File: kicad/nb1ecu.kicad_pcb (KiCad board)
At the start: 2 copper layers, 154 x 159 mm, 2 parts, among them P2 178780-1, U1 Teensy4.1

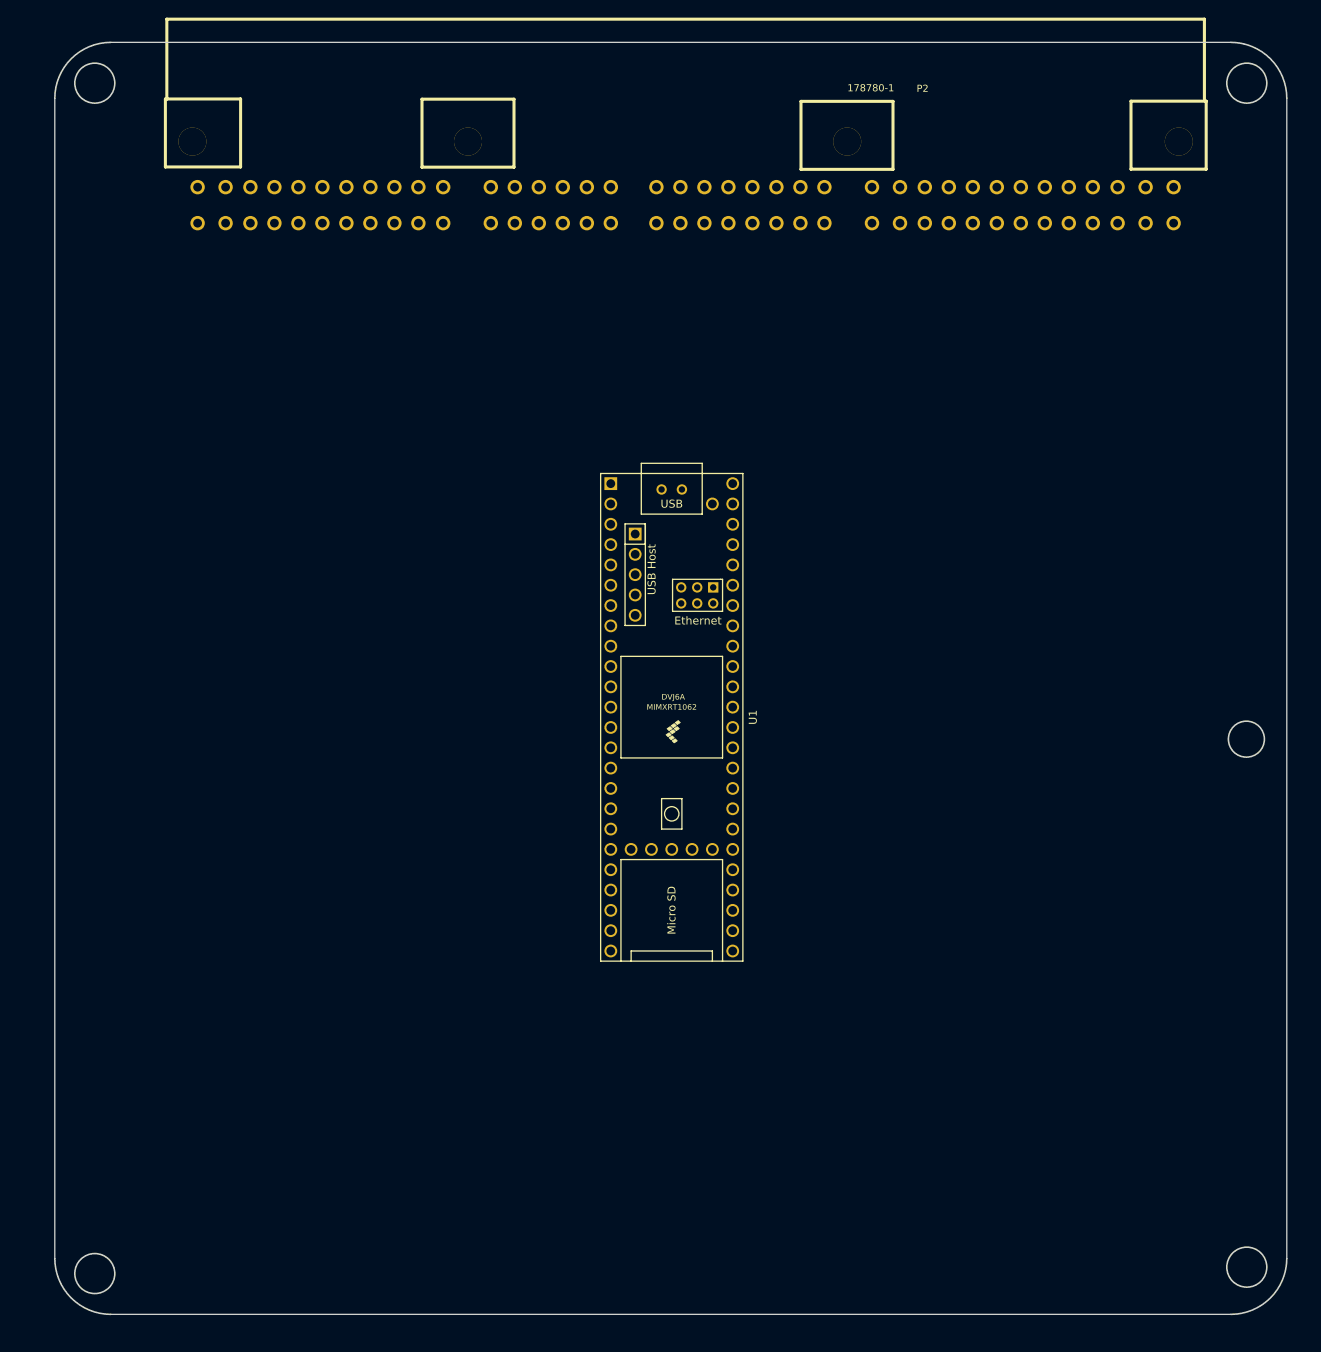
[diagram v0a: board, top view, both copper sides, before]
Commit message: ready to test, need to add part numbers for bom
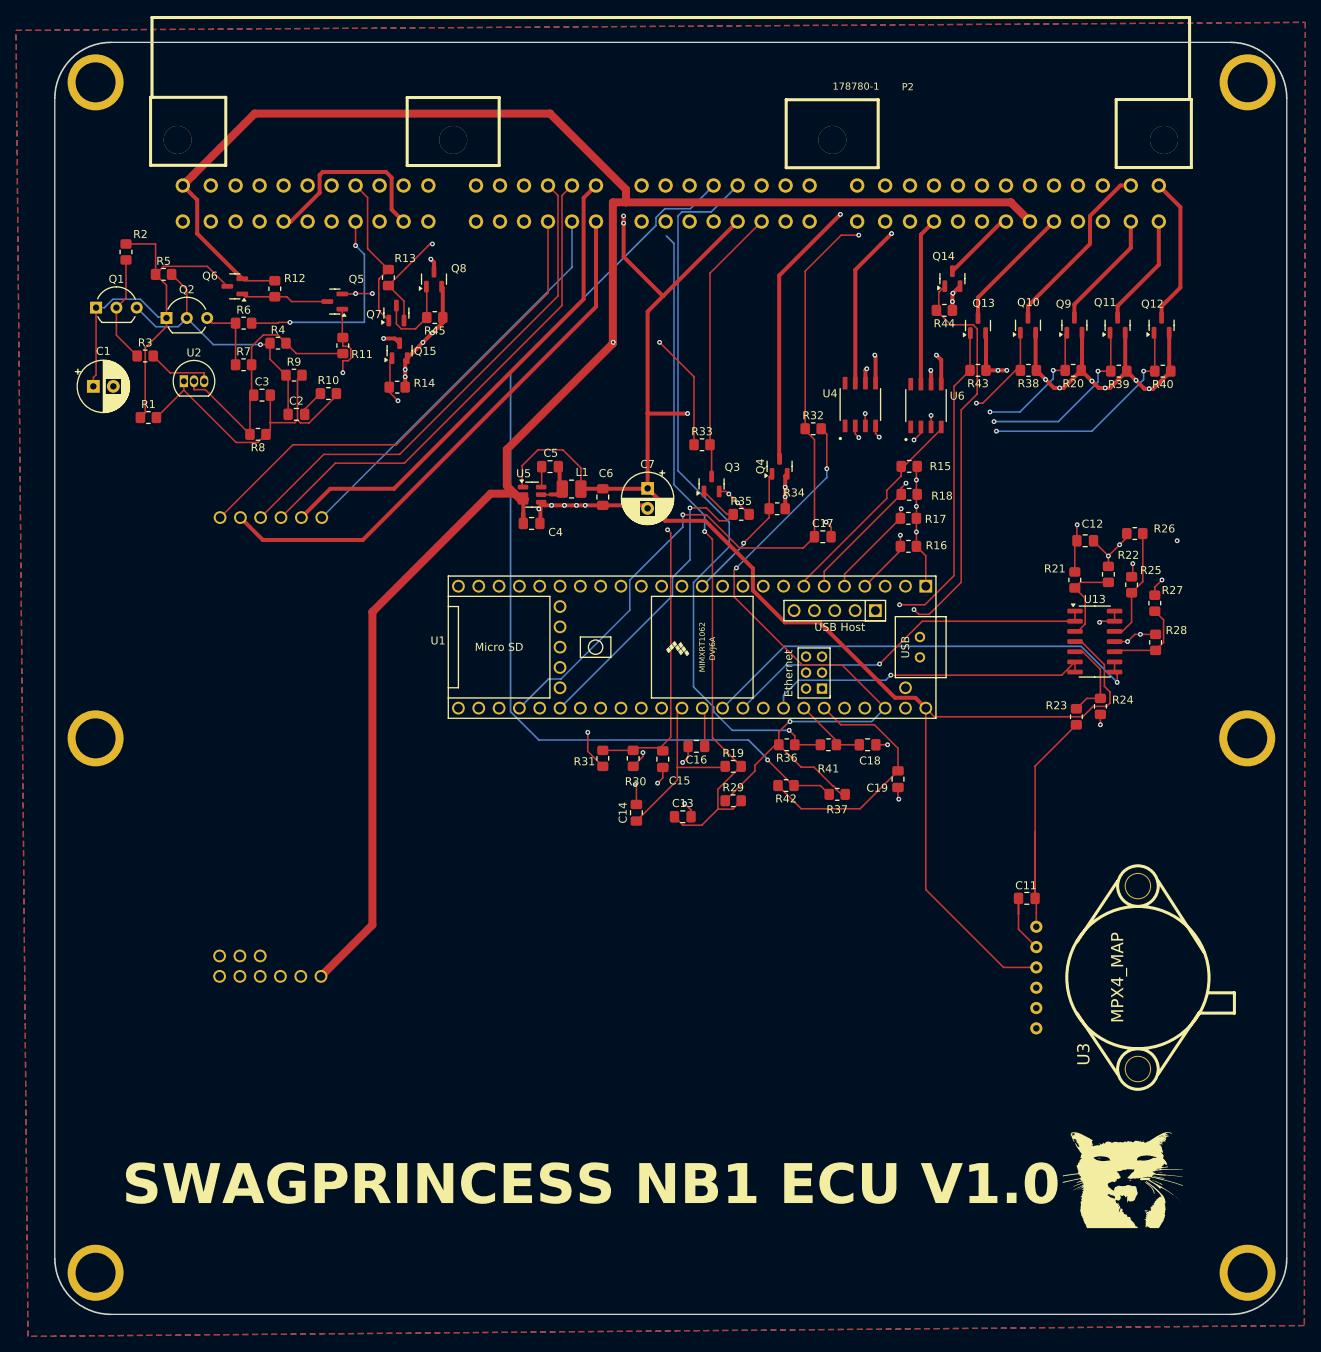
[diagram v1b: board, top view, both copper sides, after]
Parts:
- added C1: 100u, Capacitor_THT:CP_Radial_D6.3mm_P2.50mm, F.Cu at (23.4, 62.0)
- added C11: 470n, Capacitor_SMD:C_0805_2012Metric_Pad1.18x1.45mm_HandSolder, F.Cu at (140.1, 126.0)
- added C12: 220n, Capacitor_SMD:C_0805_2012Metric_Pad1.18x1.45mm_HandSolder, F.Cu at (147.4, 81.3)
- added C13: 100n, Capacitor_SMD:C_0805_2012Metric_Pad1.18x1.45mm_HandSolder, F.Cu at (97.1, 115.8)
- added C14: 220n, Capacitor_SMD:C_0805_2012Metric_Pad1.18x1.45mm_HandSolder, F.Cu at (91.3, 115.3)
- added C15: 100n, Capacitor_SMD:C_0805_2012Metric_Pad1.18x1.45mm_HandSolder, F.Cu at (94.6, 108.6)
- added C16: 220n, Capacitor_SMD:C_0805_2012Metric_Pad1.18x1.45mm_HandSolder, F.Cu at (98.8, 107.0)
- added C17: 220n, Capacitor_SMD:C_0805_2012Metric_Pad1.18x1.45mm_HandSolder, F.Cu at (114.6, 80.8)
- added C18: 100n, Capacitor_SMD:C_0805_2012Metric_Pad1.18x1.45mm_HandSolder, F.Cu at (120.2, 106.8)
- added C19: 100n, Capacitor_SMD:C_0805_2012Metric_Pad1.18x1.45mm_HandSolder, F.Cu at (124.0, 111.1)
- added C2: 22n, Capacitor_SMD:C_0805_2012Metric_Pad1.18x1.45mm_HandSolder, F.Cu at (48.8, 65.5)
- added C3: 1n, Capacitor_SMD:C_0805_2012Metric_Pad1.18x1.45mm_HandSolder, F.Cu at (44.5, 63.1)
- added C4: 10u, Capacitor_SMD:C_0805_2012Metric_Pad1.18x1.45mm_HandSolder, F.Cu at (78.2, 79.1)
- added C5: 100n, Capacitor_SMD:C_0805_2012Metric_Pad1.18x1.45mm_HandSolder, F.Cu at (80.5, 72.0)
- added C6: 10u, Capacitor_SMD:C_0805_2012Metric_Pad1.18x1.45mm_HandSolder, F.Cu at (87.1, 75.8)
- added C7: 100u, Capacitor_THT:CP_Radial_D6.3mm_P2.50mm, F.Cu at (92.7, 74.8)
- added J11: Conn_01x01, MountingHole:MountingHole_4.5mm_Pad, F.Cu at (23.7, 24.0)
- added J13: Conn_01x01, MountingHole:MountingHole_4.5mm_Pad, F.Cu at (23.7, 172.8)
- added J14: Conn_01x01, MountingHole:MountingHole_4.5mm_Pad, F.Cu at (167.7, 172.8)
- added J15: Conn_01x01, MountingHole:MountingHole_4.5mm_Pad, F.Cu at (167.7, 106.0)
- added J16: Conn_01x01, MountingHole:MountingHole_4.5mm_Pad, F.Cu at (167.7, 24.0)
- added J17: Conn_01x01, MountingHole:MountingHole_4.5mm_Pad, F.Cu at (23.7, 106.0)
- added L1: 4.7u, Inductor_SMD:L_1008_2520Metric_Pad1.43x2.20mm_HandSolder, F.Cu at (83.2, 74.8)
- added Q1: PN2907A, Package_TO_SOT_THT:TO-92_Inline_Wide, F.Cu at (23.8, 52.2)
- added Q10: DMG2302U, Package_TO_SOT_SMD:SOT-23, F.Cu at (140.2, 54.4)
- added Q11: DMG2302U, Package_TO_SOT_SMD:SOT-23, F.Cu at (151.4, 54.4)
- added Q12: DMG2302U, Package_TO_SOT_SMD:SOT-23, F.Cu at (156.9, 54.4)
- added Q13: DMG2302U, Package_TO_SOT_SMD:SOT-23, F.Cu at (134.0, 54.4)
- added Q14: DMG2302U, Package_TO_SOT_SMD:SOT-23, F.Cu at (130.8, 48.5)
- added Q15: DMG2302U, Package_TO_SOT_SMD:SOT-23, F.Cu at (61.7, 57.5)
- added Q2: PN2907A, Package_TO_SOT_THT:TO-92_Inline_Wide, F.Cu at (32.6, 53.5)
- added Q3: DMG2302U, Package_TO_SOT_SMD:SOT-23, F.Cu at (100.7, 74.2)
- added Q4: DMG2302U, Package_TO_SOT_SMD:SOT-23, F.Cu at (109.2, 72.0)
- added Q5: DMG2302U, Package_TO_SOT_SMD:SOT-23, F.Cu at (53.6, 51.4)
- added Q6: DMG2305UX, Package_TO_SOT_SMD:SOT-23, F.Cu at (41.1, 49.5)
- added Q7: DMG2305UX, Package_TO_SOT_SMD:SOT-23, F.Cu at (61.3, 52.8)
- added Q8: DMG2302U, Package_TO_SOT_SMD:SOT-23, F.Cu at (66.0, 48.6)
- added Q9: DMG2302U, Package_TO_SOT_SMD:SOT-23, F.Cu at (146.1, 54.4)
- added R1: 48.7k, Resistor_SMD:R_0805_2012Metric_Pad1.20x1.40mm_HandSolder, F.Cu at (30.3, 65.9)
- added R10: 22k, Resistor_SMD:R_0805_2012Metric_Pad1.20x1.40mm_HandSolder, F.Cu at (52.8, 62.9)
- added R11: 10k, Resistor_SMD:R_0805_2012Metric_Pad1.20x1.40mm_HandSolder, F.Cu at (54.6, 56.9)
- added R12: 10k, Resistor_SMD:R_0805_2012Metric_Pad1.20x1.40mm_HandSolder, F.Cu at (46.1, 49.8)
- added R13: 10k, Resistor_SMD:R_0805_2012Metric_Pad1.20x1.40mm_HandSolder, F.Cu at (60.3, 48.4)
- added R14: 10k, Resistor_SMD:R_0805_2012Metric_Pad1.20x1.40mm_HandSolder, F.Cu at (61.4, 62.1)
- added R15: 180k, Resistor_SMD:R_0805_2012Metric_Pad1.20x1.40mm_HandSolder, F.Cu at (125.4, 72.0)
- added R16: 180k, Resistor_SMD:R_0805_2012Metric_Pad1.20x1.40mm_HandSolder, F.Cu at (125.3, 82.0)
- added R17: 180k, Resistor_SMD:R_0805_2012Metric_Pad1.20x1.40mm_HandSolder, F.Cu at (125.3, 78.5)
- added R18: 180k, Resistor_SMD:R_0805_2012Metric_Pad1.20x1.40mm_HandSolder, F.Cu at (125.4, 75.5)
- added R19: 470, Resistor_SMD:R_0805_2012Metric_Pad1.20x1.40mm_HandSolder, F.Cu at (103.4, 109.5)
- added R2: 330, Resistor_SMD:R_0805_2012Metric_Pad1.20x1.40mm_HandSolder, F.Cu at (27.5, 45.2)
- added R20: 180k, Resistor_SMD:R_0805_2012Metric_Pad1.20x1.40mm_HandSolder, F.Cu at (145.9, 60.0)
- added R21: 180k, Resistor_SMD:R_0805_2012Metric_Pad1.20x1.40mm_HandSolder, F.Cu at (146.1, 86.2)
- added R22: 348k, Resistor_SMD:R_0805_2012Metric_Pad1.20x1.40mm_HandSolder, F.Cu at (150.3, 85.5)
- added R23: 180k, Resistor_SMD:R_0805_2012Metric_Pad1.20x1.40mm_HandSolder, F.Cu at (146.3, 103.3)
- added R24: 348k, Resistor_SMD:R_0805_2012Metric_Pad1.20x1.40mm_HandSolder, F.Cu at (149.3, 102.0)
- added R25: 180k, Resistor_SMD:R_0805_2012Metric_Pad1.20x1.40mm_HandSolder, F.Cu at (153.2, 86.8)
- added R26: 348k, Resistor_SMD:R_0805_2012Metric_Pad1.20x1.40mm_HandSolder, F.Cu at (153.6, 80.4)
- added R27: 180k, Resistor_SMD:R_0805_2012Metric_Pad1.20x1.40mm_HandSolder, F.Cu at (156.1, 89.1)
- added R28: 348k, Resistor_SMD:R_0805_2012Metric_Pad1.20x1.40mm_HandSolder, F.Cu at (156.2, 94.0)
- added R29: 2.49k, Resistor_SMD:R_0805_2012Metric_Pad1.20x1.40mm_HandSolder, F.Cu at (103.4, 113.8)
- added R3: 3.3k, Resistor_SMD:R_0805_2012Metric_Pad1.20x1.40mm_HandSolder, F.Cu at (29.9, 58.2)
- added R30: 2.49k, Resistor_SMD:R_0805_2012Metric_Pad1.20x1.40mm_HandSolder, F.Cu at (90.9, 108.5)
- added R31: 470, Resistor_SMD:R_0805_2012Metric_Pad1.20x1.40mm_HandSolder, F.Cu at (87.1, 108.5)
- added R32: 1k, Resistor_SMD:R_0805_2012Metric_Pad1.20x1.40mm_HandSolder, F.Cu at (113.4, 67.3)
- added R33: 10k, Resistor_SMD:R_0805_2012Metric_Pad1.20x1.40mm_HandSolder, F.Cu at (99.5, 69.3)
- added R34: 10k, Resistor_SMD:R_0805_2012Metric_Pad1.20x1.40mm_HandSolder, F.Cu at (108.9, 77.3)
- added R35: 10k, Resistor_SMD:R_0805_2012Metric_Pad1.20x1.40mm_HandSolder, F.Cu at (104.4, 78.0)
- added R36: 1k, Resistor_SMD:R_0805_2012Metric_Pad1.20x1.40mm_HandSolder, F.Cu at (110.1, 106.8)
- added R37: 1k, Resistor_SMD:R_0805_2012Metric_Pad1.20x1.40mm_HandSolder, F.Cu at (116.4, 113.0)
- added R38: 180k, Resistor_SMD:R_0805_2012Metric_Pad1.20x1.40mm_HandSolder, F.Cu at (140.3, 60.0)
- added R39: 180k, Resistor_SMD:R_0805_2012Metric_Pad1.20x1.40mm_HandSolder, F.Cu at (151.6, 60.1)
- added R4: 3k, Resistor_SMD:R_0805_2012Metric_Pad1.20x1.40mm_HandSolder, F.Cu at (46.5, 56.6)
- added R40: 180k, Resistor_SMD:R_0805_2012Metric_Pad1.20x1.40mm_HandSolder, F.Cu at (157.1, 60.1)
- added R41: 220, Resistor_SMD:R_0805_2012Metric_Pad1.20x1.40mm_HandSolder, F.Cu at (115.3, 106.8)
- added R42: 220, Resistor_SMD:R_0805_2012Metric_Pad1.20x1.40mm_HandSolder, F.Cu at (110.0, 111.9)
- added R43: 180k, Resistor_SMD:R_0805_2012Metric_Pad1.20x1.40mm_HandSolder, F.Cu at (134.0, 60.0)
- added R44: 180k, Resistor_SMD:R_0805_2012Metric_Pad1.20x1.40mm_HandSolder, F.Cu at (129.8, 52.5)
- added R45: 10k, Resistor_SMD:R_0805_2012Metric_Pad1.20x1.40mm_HandSolder, F.Cu at (66.1, 53.4)
- added R5: 30k, Resistor_SMD:R_0805_2012Metric_Pad1.20x1.40mm_HandSolder, F.Cu at (32.2, 48.0)
- added R6: 1k, Resistor_SMD:R_0805_2012Metric_Pad1.20x1.40mm_HandSolder, F.Cu at (42.2, 54.1)
- added R7: 3k, Resistor_SMD:R_0805_2012Metric_Pad1.20x1.40mm_HandSolder, F.Cu at (42.2, 59.3)
- added R8: 10k, Resistor_SMD:R_0805_2012Metric_Pad1.20x1.40mm_HandSolder, F.Cu at (44.0, 68.0)
- added R9: 1M, Resistor_SMD:R_0805_2012Metric_Pad1.20x1.40mm_HandSolder, F.Cu at (48.5, 60.6)
- added U13: LMV324LIDT, Package_SO:SOIC-14_3.9x8.7mm_P1.27mm, F.Cu at (148.6, 93.9)
- added U2: TL431LP, Package_TO_SOT_THT:TO-92_Inline, F.Cu at (34.7, 61.4)
- added U3: MPX4_MAP, mpx:MPX-4_MAP, F.Cu at (157.8, 135.9)
- added U4: TC4424AVOA, TC4424AVOA:SOIC127P599X175-8N, F.Cu at (119.3, 64.3)
- added U5: AP63205WU, Package_TO_SOT_SMD:TSOT-23-6, F.Cu at (78.3, 75.5)
- added U6: TC4424AVOA, TC4424AVOA:SOIC127P599X175-8N, F.Cu at (127.5, 64.4)
- added U7: ~, spartan3oem:spartan3oem, F.Cu at (57.4, 83.4)
- moved U1 9.13 mm to (98.3, 94.6), turned to 180 degrees
- moved P2 1.86 mm to (144.1, 41.4)
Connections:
- P2 pad 1: unconnected-(P2A-1A-Pad1) -> /12V_PERM
- P2 pad 10: unconnected-(P2A-1S-Pad10) -> /AC_FAN
- P2 pad 12: unconnected-(P2A-1B-Pad12) -> /12V_IGN
- P2 pad 19: unconnected-(P2A-1P-Pad19) -> /AC_SWITCH
- P2 pad 20: unconnected-(P2A-1R-Pad20) -> /MAIN_FAN
- P2 pad 25: unconnected-(P2B-2E-Pad25) -> /CLT_SENS
- P2 pad 27: unconnected-(P2B-2I-Pad27) -> +5V
- P2 pad 28: unconnected-(P2B-2K-Pad28) -> /TACH_OUT
- P2 pad 31: unconnected-(P2B-2B-Pad31) -> /IAT_SENS
- P2 pad 33: unconnected-(P2B-2F-Pad33) -> /KNOCK_SENS
- P2 pad 34: unconnected-(P2B-2H-Pad34) -> /CAM_SENS
- P2 pad 35: unconnected-(P2B-2J-Pad35) -> /CRANK_SENS
- P2 pad 39: Net-(P2C-3A) -> GND
- P2 pad 40: unconnected-(P2C-3C-Pad40) -> GND
- P2 pad 41: unconnected-(P2C-3E-Pad41) -> /TPS_5V
- P2 pad 42: unconnected-(P2C-3G-Pad42) -> /IGN1/4_OUT
- P2 pad 43: unconnected-(P2C-3I-Pad43) -> /CLUTCH
- P2 pad 45: Net-(P2C-3M) -> /IAC_OUT
- P2 pad 46: unconnected-(P2C-3O-Pad46) -> /12V_IGN
- P2 pad 47: unconnected-(P2C-3Q-Pad47) -> /VICS_OUT
- P2 pad 5: unconnected-(P2A-1I-Pad5) -> /AC_FAN
- P2 pad 50: unconnected-(P2C-3W-Pad50) -> /INJ1_OUT
- P2 pad 51: unconnected-(P2C-3Y-Pad51) -> /INJ3_OUT
- P2 pad 52: Net-(P2C-3A) -> GND
- P2 pad 54: unconnected-(P2C-3F-Pad54) -> GND
- P2 pad 55: unconnected-(P2C-3H-Pad55) -> /IGN2/3_OUT
- P2 pad 58: unconnected-(P2C-3N-Pad58) -> /PUMP_OUT
- P2 pad 59: unconnected-(P2C-3P-Pad59) -> /PUMP_OUT
- P2 pad 63: unconnected-(P2C-3X-Pad63) -> /INJ2_OUT
- P2 pad 64: unconnected-(P2C-3Z-Pad64) -> /INJ4_OUT
- P2 pad 65: unconnected-(P2D-4A-Pad65) -> GND
- P2 pad 66: unconnected-(P2D-4C-Pad66) -> /IGN4_OUT
- P2 pad 67: unconnected-(P2D-4E-Pad67) -> +5V
- P2 pad 68: unconnected-(P2D-4G-Pad68) -> /O2_VM
- P2 pad 69: unconnected-(P2D-4I-Pad69) -> /O2_IA
- P2 pad 70: unconnected-(P2D-4K-Pad70) -> /O2_HEAT-
- P2 pad 71: unconnected-(P2D-4B-Pad71) -> /IGN3_OUT
- P2 pad 72: unconnected-(P2D-4D-Pad72) -> /SPARE_ANALOG_1_IN
- P2 pad 73: unconnected-(P2D-4F-Pad73) -> /LAMBDA_5V
- P2 pad 74: unconnected-(P2D-4H-Pad74) -> /O2_UN
- P2 pad 75: unconnected-(P2D-4J-Pad75) -> /O2_IP
- P2 pad 76: unconnected-(P2D-4L-Pad76) -> /O2_HEAT+
- P2 pad 8: unconnected-(P2A-1O-Pad8) -> /ALTERNATOR_FIELD
- P2 pad 9: unconnected-(P2A-1Q-Pad9) -> /CHARGE_LAMP_OUT
- U1 pad 1: unconnected-(U1-GND-Pad1) -> GND
- U1 pad 10: unconnected-(U1-8_TX2_IN1-Pad10) -> /INJ3
- U1 pad 11: unconnected-(U1-9_OUT1C-Pad11) -> /INJ4
- U1 pad 12: unconnected-(U1-10_CS_MQSR-Pad12) -> /PUMP
- U1 pad 16: Net-(P2C-3M) -> unconnected-(U1-24_A10_TX6_SCL2-Pad16)
- U1 pad 18: unconnected-(U1-26_A12_MOSI1-Pad18) -> /CHARGE_LAMP
- U1 pad 19: unconnected-(U1-27_A13_SCK1-Pad19) -> /IAC
- U1 pad 20: unconnected-(U1-28_RX7-Pad20) -> /VICS/VVT
- U1 pad 21: unconnected-(U1-29_TX7-Pad21) -> /ALTERNATOR_ENABLE
- U1 pad 28: unconnected-(U1-36_CS-Pad28) -> /CLUTCH
- U1 pad 30: unconnected-(U1-38_CS1_IN1-Pad30) -> /TACH
- U1 pad 32: unconnected-(U1-40_A16-Pad32) -> /SPARE_ANALOG_1
- U1 pad 34: unconnected-(U1-GND-Pad34) -> GND
- U1 pad 36: unconnected-(U1-14_A0_TX3_SPDIF_OUT-Pad36) -> /IAT
- U1 pad 37: unconnected-(U1-15_A1_RX3_SPDIF_IN-Pad37) -> /CLT
- U1 pad 38: unconnected-(U1-16_A2_RX4_SCL1-Pad38) -> /LAMBDA
- U1 pad 39: unconnected-(U1-17_A3_TX4_SDA1-Pad39) -> /TPS
- U1 pad 4: unconnected-(U1-2_OUT2-Pad4) -> /IGN1/4
- U1 pad 41: unconnected-(U1-19_A5_SCL-Pad41) -> /MAP
- U1 pad 42: unconnected-(U1-20_A6_TX5_LRCLK1-Pad42) -> /CRANK
- U1 pad 43: unconnected-(U1-21_A7_RX5_BCLK1-Pad43) -> /CAM
- U1 pad 46: unconnected-(U1-3V3-Pad46) -> +3V3
- U1 pad 47: unconnected-(U1-GND-Pad47) -> GND
- U1 pad 48: unconnected-(U1-VIN-Pad48) -> +5V
- U1 pad 5: unconnected-(U1-3_LRCLK2-Pad5) -> /IGN2/3
- U1 pad 52: unconnected-(U1-GND-Pad52) -> GND
- U1 pad 58: unconnected-(U1-GND-Pad58) -> GND
- U1 pad 59: unconnected-(U1-GND-Pad59) -> GND
- U1 pad 6: unconnected-(U1-4_BCLK2-Pad6) -> /IGN3
- U1 pad 64: unconnected-(U1-GND-Pad64) -> GND
- U1 pad 7: unconnected-(U1-5_IN2-Pad7) -> /IGN4
- U1 pad 8: unconnected-(U1-6_OUT1D-Pad8) -> /INJ1
- U1 pad 9: unconnected-(U1-7_RX2_OUT1A-Pad9) -> /INJ2
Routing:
- net /12V_IGN: track 0.00 -> 280.2 mm, vias 0 -> 2
- net +5V: track 0.00 -> 279.7 mm, vias 0 -> 6
- net /LAMBDA_5V: track 0.00 -> 269.6 mm, vias 0 -> 1
- net GND: track 0.00 -> 188.6 mm, vias 0 -> 42
- net /SPARE_ANALOG_1_IN: track 0.00 -> 143.4 mm, vias 0 -> 2
- net /IAT_SENS: track 0.00 -> 134.9 mm, vias 0 -> 1
- net /CAM_SENS: track 0.00 -> 122.4 mm, vias 0 -> 1
- net +3V3: track 0.00 -> 110.0 mm, vias 0 -> 4
- net /CLUTCH: track 0.00 -> 109.1 mm, vias 0 -> 2
- net /IAC: track 0.00 -> 97.5 mm, vias 0 -> 1
- net /CRANK_SENS: track 0.00 -> 92.2 mm, vias 0 -> 1
- net /VICS/VVT: track 0.00 -> 85.4 mm, vias 0 -> 1
- net /CLT_SENS: track 0.00 -> 75.5 mm, vias 0 -> 1
- net /INJ4: track 0.00 -> 72.6 mm, vias 0 -> 2
- net /IGN3_OUT: track 0.00 -> 72.4 mm, vias 0 -> 1
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- added copper zone on B.Cu, net GND
- added copper zone on F.Cu, net GND
- added copper zone on In1.Cu, net GND
- added copper zone on In2.Cu, net GND
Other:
- outline, holes or cut-outs redrawn
- copper layers 2 -> 4
- board text added: "1A"
- board text added: "1B"
- board text added: "1C"
- board text added: "1D"
- board text added: "1E"
- board text added: "1F"
- board text added: "1G"
- board text added: "1H"
- board text added: "1I"
- board text added: "1J"
- board text added: "1K"
- board text added: "1L"
- board text added: "1M"
- board text added: "1N"
- board text added: "1O"
- board text added: "1P"
- board text added: "1Q"
- board text added: "1R"
- board text added: "1S"
- board text added: "1T"
- board text added: "1U"
- board text added: "1V"
- board text added: "2A"
- board text added: "2B"
- board text added: "2C"
- board text added: "2D"
- board text added: "2E"
- board text added: "2F"
- board text added: "2G"
- board text added: "2H"
- board text added: "2I"
- board text added: "2J"
- board text added: "2K"
- board text added: "2L"
- board text added: "2M"
- board text added: "2N"
- board text added: "2O"
- board text added: "2P"
- board text added: "3A"
- board text added: "3B"
- board text added: "3C"
- board text added: "3D"
- board text added: "3E"
- board text added: "3F"
- board text added: "3G"
- board text added: "3H"
- board text added: "3I"
- board text added: "3J"
- board text added: "3K"
- board text added: "3L"
- board text added: "3M"
- board text added: "3N"
- board text added: "3O"
- board text added: "3P"
- board text added: "3Q"
- board text added: "3R"
- board text added: "3S"
- board text added: "3T"
- board text added: "3U"
- board text added: "3V"
- board text added: "3W"
- board text added: "3X"
- board text added: "3Y"
- board text added: "3Z"
- board text added: "4A"
- board text added: "4B"
- board text added: "4C"
- board text added: "4D"
- board text added: "4E"
- board text added: "4F"
- board text added: "4G"
- board text added: "4H"
- board text added: "4I"
- board text added: "4J"
- board text added: "4K"
- board text added: "4L"
- board text added: "SWAGPRINCESS NB1 ECU V1.0"

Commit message: boost control instead of lambda output on connector and other fixes
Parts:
- removed J11, J13, J14, J15, J16, J17: Conn_01x01, MountingHole:MountingHole_4.5mm_Pad
- added J1: Conn_01x01, MountingHole:MountingHole_4.5mm_Pad, F.Cu at (167.6, 24.3)
- added J2: Conn_01x01, MountingHole:MountingHole_4.5mm_Pad, F.Cu at (167.6, 106.3)
- added J3: Conn_01x01, MountingHole:MountingHole_4.5mm_Pad, F.Cu at (167.6, 173.1)
- added J4: Conn_01x01, MountingHole:MountingHole_4.5mm_Pad, F.Cu at (23.6, 173.1)
- added J5: Conn_01x01, MountingHole:MountingHole_4.5mm_Pad, F.Cu at (23.6, 106.3)
- added J6: Conn_01x01, MountingHole:MountingHole_4.5mm_Pad, F.Cu at (23.6, 24.3)
- added LAMBDA_OUT1: TestPoint, TestPoint:TestPoint_Pad_3.0x3.0mm, F.Cu at (164.1, 85.9)
- added Q16: DMG2302U, Package_TO_SOT_SMD:SOT-23, F.Cu at (71.6, 48.5)
- added R46: 180k, Resistor_SMD:R_0805_2012Metric_Pad1.20x1.40mm_HandSolder, F.Cu at (71.6, 53.4)
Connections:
- P2 pad 67: +5V -> /12V_IGN
- P2 pad 73: /LAMBDA_5V -> /BOOST_OUT
- U1 pad 16: unconnected-(U1-24_A10_TX6_SCL2-Pad16) -> /BOOST
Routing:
- net /BOOST: track 0.00 -> 47.5 mm, vias 0 -> 1
- net /12V_IGN: track 280.2 -> 302.2 mm
- net /BOOST_OUT: track 0.00 -> 20.7 mm, vias 0 -> 3
- net /LAMBDA_5V: track 269.6 -> 276.8 mm
- net GND: track 188.6 -> 192.6 mm, vias 42 -> 44
- net +5V: track 279.7 -> 277.6 mm
- net /AC_FAN: track 32.1 -> 33.9 mm, vias 1 -> 2

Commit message: bunch of new features
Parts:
- removed Q7: DMG2305UX, Package_TO_SOT_SMD:SOT-23
- added C10: 220n, Capacitor_SMD:C_0805_2012Metric_Pad1.18x1.45mm_HandSolder, F.Cu at (60.9, 53.2)
- added C20: 100n, Capacitor_SMD:C_0805_2012Metric_Pad1.18x1.45mm_HandSolder, F.Cu at (92.6, 121.9)
- added C21: 22n, Capacitor_SMD:C_0805_2012Metric_Pad1.18x1.45mm_HandSolder, F.Cu at (79.5, 120.8)
- added C8: 100n, Capacitor_SMD:C_0805_2012Metric_Pad1.18x1.45mm_HandSolder, F.Cu at (76.0, 114.9)
- added C9: 220n, Capacitor_SMD:C_0805_2012Metric_Pad1.18x1.45mm_HandSolder, F.Cu at (79.5, 108.0)
- added Q17: DMG2302U, Package_TO_SOT_SMD:SOT-23, F.Cu at (33.4, 70.3)
- added R47: 180k, Resistor_SMD:R_0805_2012Metric_Pad1.20x1.40mm_HandSolder, F.Cu at (33.4, 74.7)
- added R48: 3.88k, Resistor_SMD:R_0805_2012Metric_Pad1.20x1.40mm_HandSolder, F.Cu at (70.7, 107.5)
- added R49: 604, Resistor_SMD:R_0805_2012Metric_Pad1.20x1.40mm_HandSolder, F.Cu at (75.0, 110.3)
- added R50: 470, Resistor_SMD:R_0805_2012Metric_Pad1.20x1.40mm_HandSolder, F.Cu at (79.8, 111.7)
- added R51: 1k, Resistor_SMD:R_0805_2012Metric_Pad1.20x1.40mm_HandSolder, F.Cu at (61.5, 50.5)
- added U8: MPXHZ6115A, Package_SO:SSOP-8_3.95x5.21x3.27mm_P1.27mm, F.Cu at (86.1, 123.7)
- R13: value 10k -> 48.7k
- U3: value MPX4_MAP -> MPX4250
- moved R13 72.5 mm to (84.7, 116.7), turned to 0 degrees
- moved U3 15.6 mm to (142.2, 136.0)
- moved C11 15.6 mm to (124.5, 126.1)
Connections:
- P2 pad 19: /AC_SWITCH -> /AC
- P2 pad 20: /MAIN_FAN -> /MAIN_FAN_OUT
- Q8 pad 1: Net-(Q7-D) -> /AC_OUT
- R13 pad 1: +5V -> /BARO
- R13 pad 2: /AC_SWITCH -> GND
- R45 pad 2: Net-(Q7-D) -> /AC_OUT
- U1 pad 17: unconnected-(U1-25_A11_RX6_SDA2-Pad17) -> /MAIN_FAN
- U1 pad 22: unconnected-(U1-30_CRX3-Pad22) -> /AC_OUT
- U1 pad 23: unconnected-(U1-31_CTX3-Pad23) -> /AC
- U1 pad 31: unconnected-(U1-39_MISO1_OUT1A-Pad31) -> /BATT
- U1 pad 40: unconnected-(U1-18_A4_SDA-Pad40) -> /BARO
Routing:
- net +3V3: track 110.0 -> 191.4 mm, vias 4 -> 5
- net /MAIN_FAN: track 0.00 -> 68.5 mm, vias 0 -> 1
- net /AC: track 0.00 -> 58.7 mm, vias 0 -> 1
- net /MAIN_FAN_OUT: track 0.00 -> 48.0 mm, vias 0 -> 3
- net /AC_OUT: track 0.00 -> 45.5 mm, vias 0 -> 1
- net /BARO: track 0.00 -> 39.3 mm, vias 0 -> 1
- net /AC_SWITCH: track 19.6 -> 0.00 mm
- net +5V: track 277.6 -> 260.4 mm, vias 6 -> 5
- net GND: track 192.6 -> 206.3 mm, vias 44 -> 53
- net Net-(C8-Pad1): track 0.00 -> 13.0 mm
- net /12V_IGN: track 302.2 -> 313.6 mm
- net /BATT: track 0.00 -> 11.2 mm
- net Net-(Q7-D): track 10.8 -> 0.00 mm
- net /MAP_5V: track 35.6 -> 33.8 mm

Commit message: options connector
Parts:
- removed LAMBDA_OUT1: TestPoint, TestPoint:TestPoint_Pad_3.0x3.0mm
- added C22: 220n, Capacitor_SMD:C_0805_2012Metric_Pad1.18x1.45mm_HandSolder, F.Cu at (141.0, 78.8)
- added J1: Conn_02x03_Top_Bottom, Connector_Molex:Molex_Micro-Fit_3.0_43045-0600_2x03_P3.00mm_Horizontal, F.Cu at (161.2, 68.8)
- added R52: 1k, Resistor_SMD:R_0805_2012Metric_Pad1.20x1.40mm_HandSolder, F.Cu at (136.3, 78.7)
- R48: value 3.88k -> 3.9k
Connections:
- U1 pad 24: unconnected-(U1-32_OUT1B-Pad24) -> /SPARE_DIGITAL_1
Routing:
- net /SPARE_DIGITAL_1: track 0.00 -> 101.4 mm, vias 0 -> 1
- net +5V: track 260.4 -> 315.5 mm
- net /12V_IGN: track 313.6 -> 352.6 mm
- net /VICS_OUT: track 16.0 -> 50.2 mm, vias 0 -> 4
- net +3V3: track 191.4 -> 219.6 mm, vias 5 -> 6
- net /LAMBDA_5V: track 276.8 -> 288.7 mm
- net /SPARE_ANALOG_1_IN: track 143.4 -> 145.3 mm
- net GND: track 206.3 -> 207.8 mm, vias 53 -> 54
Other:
- board text added: "Docs and basemaps at: https://github.com/swagprincess/ecudocumentation"
